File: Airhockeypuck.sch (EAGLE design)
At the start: 24 parts, among them J1 USB-MB-H

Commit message: completed connections
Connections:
- removed net A4/LED: LED2.A, U$1.12.A4
- net A4: now also U$1.12.A4
- net B7: now also LED2.A
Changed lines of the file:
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@@
 <net name="B4/USER" class="0">
-<segment>
-<pinref part="U$1" gate="G$1" pin="11.B4"/>
-<wire x1="15.24" y1="25.4" x2="2.54" y2="25.4" width="0.1524" layer="91"/>
-<label x="2.54" y="27.94" size="1.778" layer="95"/>
-</segment>
 <segment>
 <pinref part="R4" gate="G$1" pin="2"/>
@@
 <label x="88.9" y="0" size="1.778" layer="95"/>
 </segment>
-</net>
-<net name="A4/LED" class="0">
 <segment>
-<pinref part="U$1" gate="G$1" pin="12.A4"/>
-<wire x1="15.24" y1="20.32" x2="2.54" y2="20.32" width="0.1524" layer="91"/>
-<label x="2.54" y="22.86" size="1.778" layer="95"/>
-</segment>
-<segment>
-<pinref part="LED2" gate="G$1" pin="A"/>
-<wire x1="157.48" y1="109.22" x2="157.48" y2="119.38" width="0.1524" layer="91"/>
-<label x="157.48" y="116.84" size="1.778" layer="95"/>
+<pinref part="U$1" gate="G$1" pin="11.B4"/>
+<wire x1="15.24" y1="25.4" x2="2.54" y2="25.4" width="0.1524" layer="91"/>
+<label x="2.54" y="27.94" size="1.778" layer="95"/>
 </segment>
 </net>
@@
 <label x="203.2" y="0" size="1.778" layer="95"/>
 </segment>
+<segment>
+<pinref part="LED2" gate="G$1" pin="A"/>
+<wire x1="157.48" y1="109.22" x2="157.48" y2="119.38" width="0.1524" layer="91"/>
+<label x="157.48" y="116.84" size="1.778" layer="95"/>
+</segment>
 </net>
 <net name="D+" class="0">
@@
 <label x="203.2" y="2.54" size="1.778" layer="95"/>
 </segment>
+<segment>
+<pinref part="U$1" gate="G$1" pin="12.A4"/>
+<wire x1="15.24" y1="20.32" x2="2.54" y2="20.32" width="0.1524" layer="91"/>
+<label x="2.54" y="22.86" size="1.778" layer="95"/>
+</segment>
 </net>

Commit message: minor edits
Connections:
- new net N$8: C4.1, U$2.2, U$3.2.VIN
- net +5V: no longer C4.1, U$2.2, U$3.2.VIN
- net GND: now also J1.GND
- net USBID: no longer J1.GND
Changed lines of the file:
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@@
 <part name="GND7" library="MEE_433" deviceset="GND" device=""/>
 <part name="GND8" library="MEE_433" deviceset="GND" device=""/>
-<part name="GND9" library="MEE_433" deviceset="GND" device=""/>
 <part name="GND10" library="MEE_433" deviceset="GND" device=""/>
 <part name="GND11" library="MEE_433" deviceset="GND" device=""/>
@@
 <part name="GND16" library="MEE_433" deviceset="GND" device=""/>
 <part name="GND17" library="MEE_433" deviceset="GND" device=""/>
-<part name="P+1" library="MEE_433" deviceset="+5V" device=""/>
 <part name="P+2" library="MEE_433" deviceset="+5V" device=""/>
 <part name="U$1" library="MEE_433" deviceset="PIC32MX250F128B" device=""/>
@@
 <part name="+3V11" library="MEE_433" deviceset="+3V3" device=""/>
 <part name="GND21" library="MEE_433" deviceset="GND" device=""/>
+<part name="GND9" library="MEE_433" deviceset="GND" device=""/>
 </parts>
 <sheets>
@@
 <attribute name="VALUE" x="76.2" y="66.04" size="1.778" layer="96"/>
 </instance>
-<instance part="GND9" gate="1" x="30.48" y="111.76" smashed="yes" rot="R180">
-<attribute name="VALUE" x="33.02" y="114.3" size="1.778" layer="96" rot="R180"/>
-</instance>
 <instance part="GND10" gate="1" x="71.12" y="91.44" smashed="yes">
 <attribute name="VALUE" x="68.58" y="88.9" size="1.778" layer="96"/>
@@
 <instance part="GND17" gate="1" x="124.46" y="-2.54" smashed="yes">
 <attribute name="VALUE" x="121.92" y="-5.08" size="1.778" layer="96"/>
-</instance>
-<instance part="P+1" gate="1" x="66.04" y="111.76" smashed="yes">
-<attribute name="VALUE" x="63.5" y="106.68" size="1.778" layer="96" rot="R90"/>
 </instance>
 <instance part="P+2" gate="1" x="78.74" y="15.24" smashed="yes">
@@
 <attribute name="VALUE" x="86.36" y="48.26" size="1.778" layer="96" rot="R90"/>
 </instance>
-<instance part="P+4" gate="1" x="55.88" y="111.76" smashed="yes">
-<attribute name="VALUE" x="53.34" y="106.68" size="1.778" layer="96" rot="R90"/>
-</instance>
+<instance part="P+4" gate="1" x="55.88" y="111.76" smashed="yes"/>
 <instance part="U$10" gate="G$1" x="157.48" y="60.96" smashed="yes"/>
 <instance part="GND20" gate="1" x="187.96" y="63.5" smashed="yes">
@@
 <instance part="GND21" gate="1" x="160.02" y="33.02" smashed="yes">
 <attribute name="VALUE" x="157.48" y="30.48" size="1.778" layer="96"/>
+</instance>
+<instance part="GND9" gate="1" x="30.48" y="114.3" smashed="yes" rot="R180">
+<attribute name="VALUE" x="33.02" y="116.84" size="1.778" layer="96" rot="R180"/>
 </instance>
 </instances>
@@
 <wire x1="144.78" y1="35.56" x2="160.02" y2="35.56" width="0.1524" layer="91"/>
 <pinref part="GND21" gate="1" pin="GND"/>
+</segment>
+<segment>
+<pinref part="J1" gate="G$1" pin="GND"/>
+<wire x1="25.4" y1="109.22" x2="30.48" y2="109.22" width="0.1524" layer="91"/>
+<wire x1="30.48" y1="109.22" x2="30.48" y2="111.76" width="0.1524" layer="91"/>
+<pinref part="GND9" gate="1" pin="GND"/>
 </segment>
 </net>
@@
 </segment>
 <segment>
-<pinref part="U$3" gate="G$1" pin="2.VIN"/>
-<pinref part="C4" gate="G$1" pin="1"/>
-<wire x1="71.12" y1="109.22" x2="78.74" y2="109.22" width="0.1524" layer="91"/>
-<junction x="71.12" y="109.22"/>
-<wire x1="66.04" y1="109.22" x2="71.12" y2="109.22" width="0.1524" layer="91"/>
-<pinref part="P+1" gate="1" pin="+5V"/>
-<wire x1="66.04" y1="109.22" x2="60.96" y2="109.22" width="0.1524" layer="91"/>
-<junction x="66.04" y="109.22"/>
-<wire x1="60.96" y1="109.22" x2="60.96" y2="116.84" width="0.1524" layer="91"/>
-<wire x1="60.96" y1="116.84" x2="50.8" y2="116.84" width="0.1524" layer="91"/>
-<pinref part="U$2" gate="G$1" pin="2"/>
-<wire x1="50.8" y1="116.84" x2="50.8" y2="109.22" width="0.1524" layer="91"/>
-</segment>
-<segment>
 <pinref part="P+4" gate="1" pin="+5V"/>
 <pinref part="U$2" gate="G$1" pin="1"/>
@@
 </segment>
 <segment>
-<pinref part="GND9" gate="1" pin="GND"/>
 <pinref part="J1" gate="G$1" pin="ID"/>
-<pinref part="J1" gate="G$1" pin="GND"/>
-<wire x1="25.4" y1="109.22" x2="30.48" y2="109.22" width="0.1524" layer="91"/>
 <wire x1="25.4" y1="99.06" x2="35.56" y2="99.06" width="0.1524" layer="91"/>
 <label x="27.94" y="99.06" size="1.778" layer="95"/>
@@
 </segment>
 </net>
+<net name="N$8" class="0">
+<segment>
+<pinref part="U$3" gate="G$1" pin="2.VIN"/>
+<pinref part="C4" gate="G$1" pin="1"/>
+<wire x1="71.12" y1="109.22" x2="78.74" y2="109.22" width="0.1524" layer="91"/>
+<junction x="71.12" y="109.22"/>
+<wire x1="71.12" y1="109.22" x2="60.96" y2="109.22" width="0.1524" layer="91"/>
+<wire x1="60.96" y1="109.22" x2="60.96" y2="116.84" width="0.1524" layer="91"/>
+<wire x1="60.96" y1="116.84" x2="50.8" y2="116.84" width="0.1524" layer="91"/>
+<pinref part="U$2" gate="G$1" pin="2"/>
+<wire x1="50.8" y1="116.84" x2="50.8" y2="109.22" width="0.1524" layer="91"/>
+</segment>
+</net>

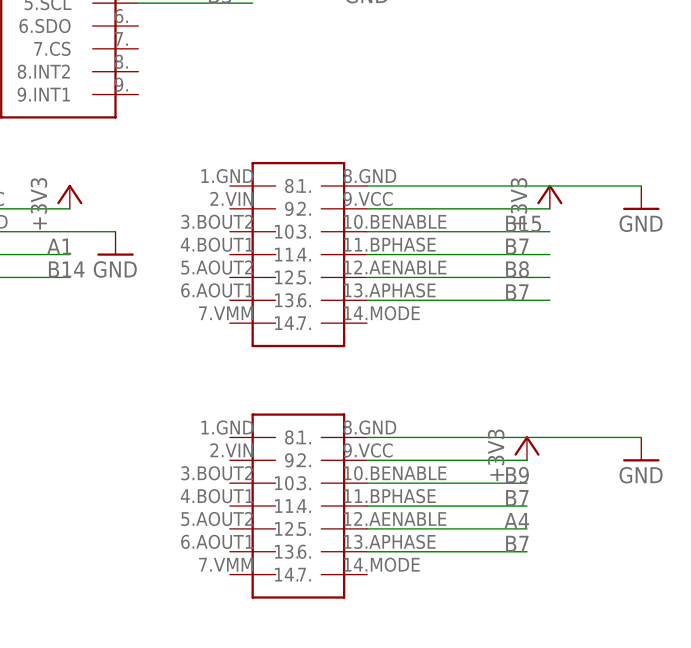
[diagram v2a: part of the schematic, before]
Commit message: Changed device DRV8835
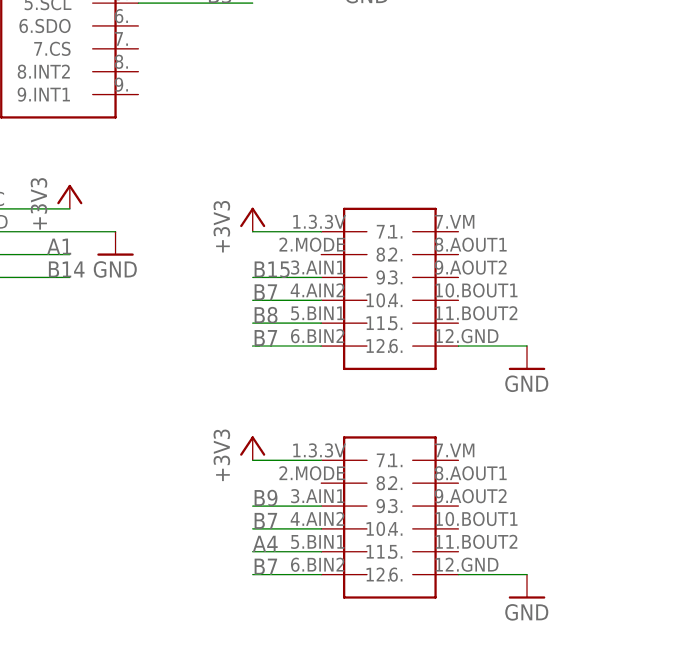
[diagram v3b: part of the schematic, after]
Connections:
- net +3V3: now also U$6.1., U$7.1.; no longer U$6.9., U$7.9.
- net A4: now also U$7.5.; no longer U$7.12.
- net B15: now also U$6.3.; no longer U$6.10.
- net B7: now also U$6.4., U$6.6., U$7.4., U$7.6.; no longer U$6.11., U$6.13., U$7.11., U$7.13.
- net B8: now also U$6.5.; no longer U$6.12.
- net B9: now also U$7.3.; no longer U$7.10.
- net GND: now also U$6.12., U$7.12.; no longer U$6.8., U$7.8.
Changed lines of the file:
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@@
 <part name="GND20" library="MEE_433" deviceset="GND" device=""/>
 <part name="+3V9" library="MEE_433" deviceset="+3V3" device=""/>
-<part name="U$6" library="MEE_433" deviceset="DRV8835" device=""/>
-<part name="U$7" library="MEE_433" deviceset="DRV8835" device=""/>
-<part name="GND18" library="MEE_433" deviceset="GND" device=""/>
-<part name="GND19" library="MEE_433" deviceset="GND" device=""/>
-<part name="+3V7" library="MEE_433" deviceset="+3V3" device=""/>
-<part name="+3V10" library="MEE_433" deviceset="+3V3" device=""/>
 <part name="U$11" library="MEE_433" deviceset="HC-08" device=""/>
 <part name="+3V11" library="MEE_433" deviceset="+3V3" device=""/>
 <part name="GND21" library="MEE_433" deviceset="GND" device=""/>
 <part name="GND9" library="MEE_433" deviceset="GND" device=""/>
+<part name="U$6" library="MEE_433" deviceset="DRV8835" device=""/>
+<part name="+3V7" library="MEE_433" deviceset="+3V3" device=""/>
+<part name="GND18" library="MEE_433" deviceset="GND" device=""/>
+<part name="U$7" library="MEE_433" deviceset="DRV8835" device=""/>
+<part name="+3V10" library="MEE_433" deviceset="+3V3" device=""/>
+<part name="GND19" library="MEE_433" deviceset="GND" device=""/>
 </parts>
 <sheets>
@@
 <attribute name="VALUE" x="185.42" y="66.04" size="1.778" layer="96" rot="R90"/>
 </instance>
-<instance part="U$6" gate="G$1" x="180.34" y="35.56" smashed="yes"/>
-<instance part="U$7" gate="G$1" x="180.34" y="7.62" smashed="yes"/>
-<instance part="GND18" gate="1" x="218.44" y="38.1" smashed="yes">
-<attribute name="VALUE" x="215.9" y="35.56" size="1.778" layer="96"/>
-</instance>
-<instance part="GND19" gate="1" x="218.44" y="10.16" smashed="yes">
-<attribute name="VALUE" x="215.9" y="7.62" size="1.778" layer="96"/>
-</instance>
-<instance part="+3V7" gate="G$1" x="205.74" y="12.7" smashed="yes">
-<attribute name="VALUE" x="203.2" y="7.62" size="1.778" layer="96" rot="R90"/>
-</instance>
-<instance part="+3V10" gate="G$1" x="208.28" y="40.64" smashed="yes">
-<attribute name="VALUE" x="205.74" y="35.56" size="1.778" layer="96" rot="R90"/>
-</instance>
 <instance part="U$11" gate="G$1" x="142.24" y="35.56" smashed="yes"/>
 <instance part="+3V11" gate="G$1" x="154.94" y="40.64" smashed="yes">
@@
 <instance part="GND9" gate="1" x="30.48" y="114.3" smashed="yes" rot="R180">
 <attribute name="VALUE" x="33.02" y="116.84" size="1.778" layer="96" rot="R180"/>
+</instance>
+<instance part="U$6" gate="G$1" x="190.5" y="33.02" smashed="yes"/>
+<instance part="+3V7" gate="G$1" x="175.26" y="38.1" smashed="yes">
+<attribute name="VALUE" x="172.72" y="33.02" size="1.778" layer="96" rot="R90"/>
+</instance>
+<instance part="GND18" gate="1" x="205.74" y="20.32" smashed="yes">
+<attribute name="VALUE" x="203.2" y="17.78" size="1.778" layer="96"/>
+</instance>
+<instance part="U$7" gate="G$1" x="190.5" y="7.62" smashed="yes"/>
+<instance part="+3V10" gate="G$1" x="175.26" y="12.7" smashed="yes">
+<attribute name="VALUE" x="172.72" y="7.62" size="1.778" layer="96" rot="R90"/>
+</instance>
+<instance part="GND19" gate="1" x="205.74" y="-5.08" smashed="yes">
+<attribute name="VALUE" x="203.2" y="-7.62" size="1.778" layer="96"/>
 </instance>
 </instances>
@@
 </segment>
 <segment>
-<pinref part="U$6" gate="G$1" pin="8."/>
-<wire x1="187.96" y1="40.64" x2="218.44" y2="40.64" width="0.1524" layer="91"/>
-<pinref part="GND18" gate="1" pin="GND"/>
-</segment>
-<segment>
-<pinref part="U$7" gate="G$1" pin="8."/>
-<wire x1="187.96" y1="12.7" x2="218.44" y2="12.7" width="0.1524" layer="91"/>
-<pinref part="GND19" gate="1" pin="GND"/>
-</segment>
-<segment>
 <pinref part="U$11" gate="G$1" pin="2.GND"/>
 <wire x1="144.78" y1="35.56" x2="160.02" y2="35.56" width="0.1524" layer="91"/>
@@
 <wire x1="30.48" y1="109.22" x2="30.48" y2="111.76" width="0.1524" layer="91"/>
 <pinref part="GND9" gate="1" pin="GND"/>
+</segment>
+<segment>
+<pinref part="U$6" gate="G$1" pin="12."/>
+<wire x1="198.12" y1="22.86" x2="205.74" y2="22.86" width="0.1524" layer="91"/>
+<pinref part="GND18" gate="1" pin="GND"/>
+</segment>
+<segment>
+<pinref part="U$7" gate="G$1" pin="12."/>
+<wire x1="198.12" y1="-2.54" x2="205.74" y2="-2.54" width="0.1524" layer="91"/>
+<pinref part="GND19" gate="1" pin="GND"/>
 </segment>
 </net>
@@
 </segment>
 <segment>
-<pinref part="U$7" gate="G$1" pin="9."/>
-<wire x1="187.96" y1="10.16" x2="205.74" y2="10.16" width="0.1524" layer="91"/>
+<pinref part="U$6" gate="G$1" pin="1."/>
+<wire x1="182.88" y1="35.56" x2="175.26" y2="35.56" width="0.1524" layer="91"/>
 <pinref part="+3V7" gate="G$1" pin="+3V3"/>
 </segment>
 <segment>
-<pinref part="U$6" gate="G$1" pin="9."/>
-<wire x1="187.96" y1="38.1" x2="208.28" y2="38.1" width="0.1524" layer="91"/>
+<pinref part="U$7" gate="G$1" pin="1."/>
+<wire x1="182.88" y1="10.16" x2="175.26" y2="10.16" width="0.1524" layer="91"/>
 <pinref part="+3V10" gate="G$1" pin="+3V3"/>
 </segment>
@@
 </segment>
 <segment>
-<pinref part="U$6" gate="G$1" pin="10."/>
-<wire x1="187.96" y1="35.56" x2="208.28" y2="35.56" width="0.1524" layer="91"/>
-<label x="203.2" y="35.56" size="1.778" layer="95"/>
+<pinref part="U$6" gate="G$1" pin="3."/>
+<wire x1="182.88" y1="30.48" x2="175.26" y2="30.48" width="0.1524" layer="91"/>
+<label x="175.26" y="30.48" size="1.778" layer="95"/>
 </segment>
 </net>
@@
 </segment>
 <segment>
-<pinref part="U$7" gate="G$1" pin="10."/>
-<wire x1="187.96" y1="7.62" x2="205.74" y2="7.62" width="0.1524" layer="91"/>
-<label x="203.2" y="7.62" size="1.778" layer="95"/>
+<pinref part="U$7" gate="G$1" pin="3."/>
+<wire x1="182.88" y1="5.08" x2="175.26" y2="5.08" width="0.1524" layer="91"/>
+<label x="175.26" y="5.08" size="1.778" layer="95"/>
 </segment>
 </net>
@@
 </segment>
 <segment>
-<pinref part="U$6" gate="G$1" pin="12."/>
-<wire x1="187.96" y1="30.48" x2="208.28" y2="30.48" width="0.1524" layer="91"/>
-<label x="203.2" y="30.48" size="1.778" layer="95"/>
+<pinref part="U$6" gate="G$1" pin="5."/>
+<wire x1="182.88" y1="25.4" x2="175.26" y2="25.4" width="0.1524" layer="91"/>
+<label x="175.26" y="25.4" size="1.778" layer="95"/>
 </segment>
 </net>
@@
 </segment>
 <segment>
-<pinref part="U$6" gate="G$1" pin="11."/>
-<wire x1="187.96" y1="33.02" x2="208.28" y2="33.02" width="0.1524" layer="91"/>
-<label x="203.2" y="33.02" size="1.778" layer="95"/>
-</segment>
-<segment>
-<pinref part="U$6" gate="G$1" pin="13."/>
-<wire x1="187.96" y1="27.94" x2="208.28" y2="27.94" width="0.1524" layer="91"/>
-<label x="203.2" y="27.94" size="1.778" layer="95"/>
-</segment>
-<segment>
-<pinref part="U$7" gate="G$1" pin="11."/>
-<wire x1="187.96" y1="5.08" x2="205.74" y2="5.08" width="0.1524" layer="91"/>
-<label x="203.2" y="5.08" size="1.778" layer="95"/>
-</segment>
-<segment>
-<pinref part="U$7" gate="G$1" pin="13."/>
-<wire x1="187.96" y1="0" x2="205.74" y2="0" width="0.1524" layer="91"/>
-<label x="203.2" y="0" size="1.778" layer="95"/>
-</segment>
-<segment>
 <pinref part="LED2" gate="G$1" pin="A"/>
 <wire x1="157.48" y1="109.22" x2="157.48" y2="119.38" width="0.1524" layer="91"/>
 <label x="157.48" y="116.84" size="1.778" layer="95"/>
+</segment>
+<segment>
+<pinref part="U$6" gate="G$1" pin="4."/>
+<wire x1="182.88" y1="27.94" x2="175.26" y2="27.94" width="0.1524" layer="91"/>
+<label x="175.26" y="27.94" size="1.778" layer="95"/>
+</segment>
+<segment>
+<pinref part="U$6" gate="G$1" pin="6."/>
+<wire x1="182.88" y1="22.86" x2="175.26" y2="22.86" width="0.1524" layer="91"/>
+<label x="175.26" y="22.86" size="1.778" layer="95"/>
+</segment>
+<segment>
+<pinref part="U$7" gate="G$1" pin="4."/>
+<wire x1="182.88" y1="2.54" x2="175.26" y2="2.54" width="0.1524" layer="91"/>
+<label x="175.26" y="2.54" size="1.778" layer="95"/>
+</segment>
+<segment>
+<pinref part="U$7" gate="G$1" pin="6."/>
+<wire x1="182.88" y1="-2.54" x2="175.26" y2="-2.54" width="0.1524" layer="91"/>
+<label x="175.26" y="-2.54" size="1.778" layer="95"/>
 </segment>
 </net>
@@
 <net name="A4" class="0">
 <segment>
-<pinref part="U$7" gate="G$1" pin="12."/>
-<wire x1="187.96" y1="2.54" x2="205.74" y2="2.54" width="0.1524" layer="91"/>
-<label x="203.2" y="2.54" size="1.778" layer="95"/>
-</segment>
-<segment>
 <pinref part="U$1" gate="G$1" pin="12.A4"/>
 <wire x1="15.24" y1="20.32" x2="2.54" y2="20.32" width="0.1524" layer="91"/>
 <label x="2.54" y="22.86" size="1.778" layer="95"/>
 </segment>
-</net>
+<segment>
+<pinref part="U$7" gate="G$1" pin="5."/>
+<wire x1="182.88" y1="0" x2="175.26" y2="0" width="0.1524" layer="91"/>
+<label x="175.26" y="0" size="1.778" layer="95"/>
+</segment>
+</net>
